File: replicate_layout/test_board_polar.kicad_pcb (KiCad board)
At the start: 2 copper layers, 30 parts, among them J1001 Pusa_4mm, J1002 Pusa_4mm, Q1001 CSD19531KCS, Q1002 CSD19531KCS, Q1003 CSD19531KCS, Q2001 CSD19531KCS, Q2002 CSD19531KCS, Q3001 CSD19531KCS, Q3002 CSD19531KCS, Q4001 CSD19531KCS, Q4002 CSD19531KCS, U1001 LAUNCHXL-F28377S, U2001 IR2181, U3001 IR2181, U4001 IR2181

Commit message: polarna replikacija dela GUI še ne dela samo še zone je treba replicirati
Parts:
- moved Q4002 68.7 mm to (220.0, 154.0), turned to 240 degrees
- moved R4002 62.8 mm to (216.0, 151.6), turned to 330 degrees
- moved Q4001 58.4 mm to (225.4, 144.6), turned to 240 degrees
- moved R4001 51.2 mm to (221.3, 142.3), turned to 330 degrees
- moved C4002 49.6 mm to (214.7, 144.0), turned to 240 degrees
- moved U4001 44.8 mm to (209.9, 142.3), turned to 330 degrees
- moved D4001 39.8 mm to (211.8, 139.0), turned to 150 degrees
- moved C4001 38.3 mm to (205.4, 138.6), turned to 240 degrees
- moved Q3002 27.6 mm to (222.9, 110.5), turned to 300 degrees
- moved Q3001 23.9 mm to (217.5, 101.2), turned to 300 degrees
- moved R3002 23.7 mm to (218.8, 112.9), turned to 30 degrees
- moved R3001 19.3 mm to (213.4, 103.5), turned to 30 degrees
- moved C3002 16.4 mm to (211.6, 110.2), turned to 300 degrees
- moved U3001 12.9 mm to (207.7, 113.4), turned to 30 degrees
- moved D3001 10.5 mm to (205.8, 110.1), turned to 210 degrees
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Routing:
- net (no net): track 0.00 -> 19.9 mm
- net /Veja_2/OUT: track 28.1 -> 44.0 mm
- net +VDC: track 27.2 -> 39.8 mm
- net GND: track 147.8 -> 158.6 mm
- net /Veja_3/OUT: track 40.2 -> 44.0 mm
- removed copper zone on F.Cu, net /Veja_1/OUT
- removed copper zone on F.Cu, net /Veja_2/OUT
- removed copper zone on F.Cu, net /Veja_3/OUT
- removed copper zone on F.Cu, net GND

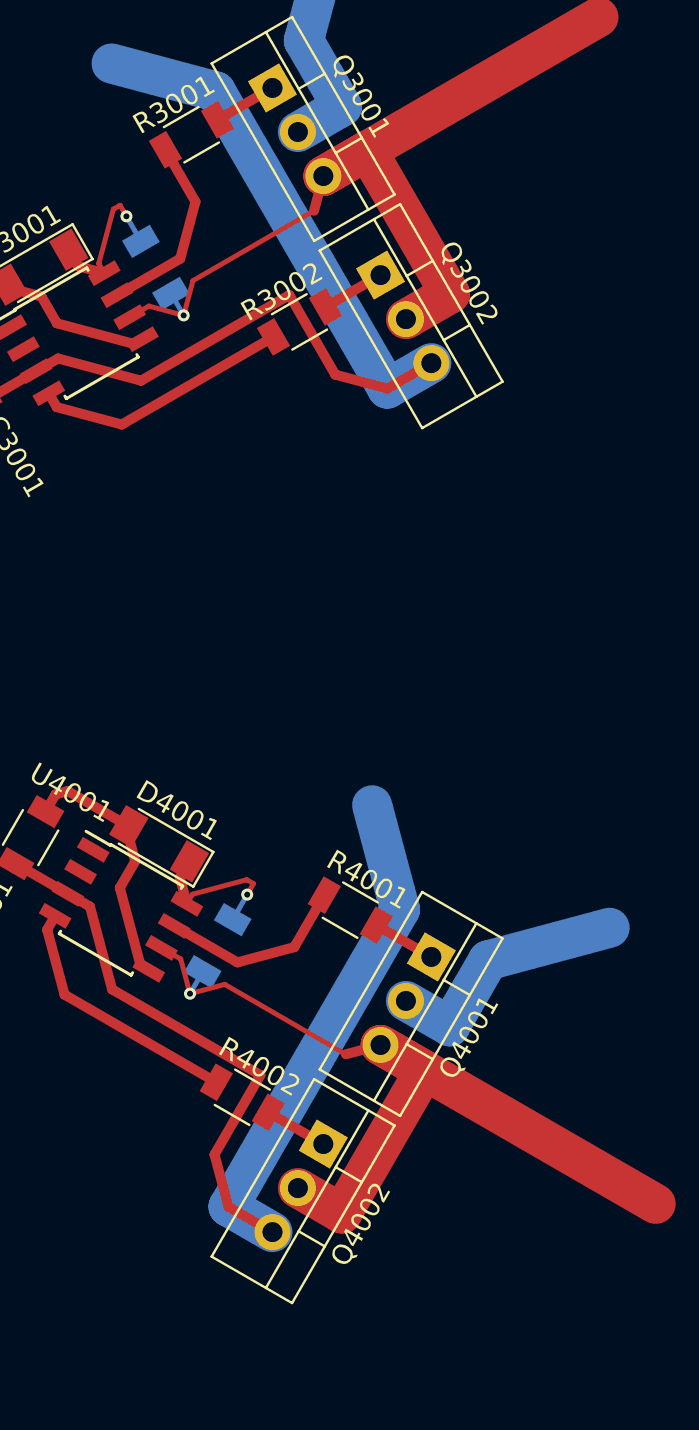
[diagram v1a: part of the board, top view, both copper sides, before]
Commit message: fixed a bug in test function changed how bounding box is calculated
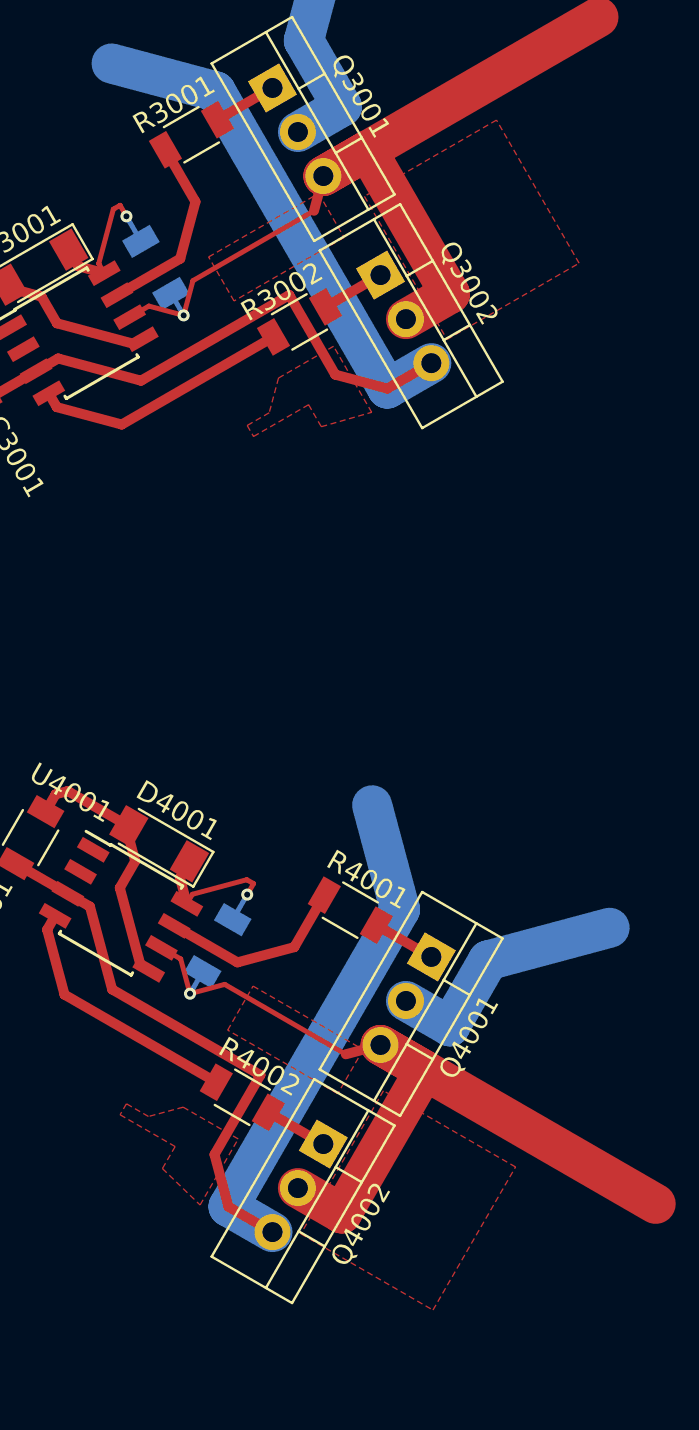
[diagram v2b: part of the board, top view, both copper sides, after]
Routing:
- added copper zone on F.Cu, net /Veja_2/OUT
- added copper zone on F.Cu, net /Veja_3/OUT
- added copper zone on F.Cu, net GND
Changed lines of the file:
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@@
-(kicad_pcb (version 20170919) (host pcbnew "(revision)-makepkg")
+(kicad_pcb (version 20170919) (host pcbnew "(2017-09-19 revision dddaa7e69)-makepkg")
   (general
     (thickness 1.6)
@@
   (segment (start 186.69 101.29) (end 184.315 103.665) (width 0.5) (layer F.Cu) (net 25))
   (segment (start 184.315 103.665) (end 183.515 103.665) (width 0.5) (layer F.Cu) (net 25))
+  (zone (net 4) (net_name /Veja_2/OUT) (layer F.Cu) (hatch edge 0.508)
+    (connect_pads (clearance 0.508))
+    (min_thickness 0.254)
+    (fill (arc_segments 16) (thermal_gap 0.508) (thermal_bridge_width 0.508))
+    (polygon
+      (pts
+        (xy 219.767651 106.459008) (xy 221.037651 108.658713) (xy 215.53839 111.833713) (xy 214.26839 109.634008)
+      )
+    )
+  )
+  (zone (net 2) (net_name GND) (layer F.Cu) (hatch edge 0.508)
+    (connect_pads (clearance 0.508))
+    (min_thickness 0.254)
+    (fill (arc_segments 16) (thermal_gap 0.508) (thermal_bridge_width 0.508))
+    (polygon
+      (pts
+        (xy 215.748021 153.698195) (xy 212.99839 152.110695) (xy 211.263538 152.575548) (xy 210.163685 151.940548) (xy 209.846185 152.490474)
+        (xy 212.595816 154.077974) (xy 211.960816 155.177826) (xy 213.843021 156.997752)
+      )
+    )
+  )
+  (zone (net 13) (net_name /Veja_3/OUT) (layer F.Cu) (hatch edge 0.508)
+    (connect_pads (clearance 0.508))
+    (min_thickness 0.254)
+    (fill (arc_segments 16) (thermal_gap 0.508) (thermal_bridge_width 0.508))
+    (polygon
+      (pts
+        (xy 229.604043 155.09886) (xy 223.00493 151.28886) (xy 218.87743 158.4379) (xy 225.476543 162.2479)
+      )
+    )
+  )
+  (zone (net 13) (net_name /Veja_3/OUT) (layer F.Cu) (hatch edge 0.508)
+    (connect_pads (clearance 0.508))
+    (min_thickness 0.254)
+    (fill (arc_segments 16) (thermal_gap 0.508) (thermal_bridge_width 0.508))
+    (polygon
+      (pts
+        (xy 221.990151 149.236508) (xy 220.720151 151.436213) (xy 215.22089 148.261213) (xy 216.49089 146.061508)
+      )
+    )
+  )
+  (zone (net 2) (net_name GND) (layer F.Cu) (hatch edge 0.508)
+    (connect_pads (clearance 0.508))
+    (min_thickness 0.254)
+    (fill (arc_segments 16) (thermal_gap 0.508) (thermal_bridge_width 0.508))
+    (polygon
+      (pts
+        (xy 220.510521 114.095695) (xy 217.76089 115.683195) (xy 217.296038 117.418048) (xy 216.196185 118.053048) (xy 216.513685 118.602974)
+        (xy 219.263316 117.015474) (xy 219.898316 118.115326) (xy 222.415521 117.395252)
+      )
+    )
+  )
+  (zone (net 4) (net_name /Veja_2/OUT) (layer F.Cu) (hatch edge 0.508)
+    (connect_pads (clearance 0.508))
+    (min_thickness 0.254)
+    (fill (arc_segments 16) (thermal_gap 0.508) (thermal_bridge_width 0.508))
+    (polygon
+      (pts
+        (xy 228.651543 102.79636) (xy 222.05243 106.60636) (xy 226.17993 113.7554) (xy 232.779043 109.9454)
+      )
+    )
+  )
 )

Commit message: Updated documentation
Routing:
- added copper zone on F.Cu, net /Veja_1/OUT
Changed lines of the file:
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@@
     (connect_pads (clearance 0.508))
     (min_thickness 0.254)
-    (fill (arc_segments 16) (thermal_gap 0.508) (thermal_bridge_width 0.508))
+    (fill yes (arc_segments 16) (thermal_gap 0.508) (thermal_bridge_width 0.508))
     (polygon
       (pts
-        (xy 220.510521 114.095695) (xy 217.76089 115.683195) (xy 217.296038 117.418048) (xy 216.196185 118.053048) (xy 216.513685 118.602974)
-        (xy 219.263316 117.015474) (xy 219.898316 118.115326) (xy 222.415521 117.395252)
+        (xy 188.595 90.17) (xy 188.595 93.345) (xy 189.865 94.615) (xy 189.865 95.885) (xy 190.5 95.885)
+        (xy 190.5 92.71) (xy 191.77 92.71) (xy 192.405 90.17)
       )
     )
@@
       )
     )
+  )
+  (zone (net 2) (net_name GND) (layer F.Cu) (hatch edge 0.508)
+    (connect_pads (clearance 0.508))
+    (min_thickness 0.254)
+    (fill (arc_segments 16) (thermal_gap 0.508) (thermal_bridge_width 0.508))
+    (polygon
+      (pts
+        (xy 220.510521 114.095695) (xy 217.76089 115.683195) (xy 217.296038 117.418048) (xy 216.196185 118.053048) (xy 216.513685 118.602974)
+        (xy 219.263316 117.015474) (xy 219.898316 118.115326) (xy 222.415521 117.395252)
+      )
+    )
+  )
+  (zone (net 3) (net_name /Veja_1/OUT) (layer F.Cu) (hatch edge 0.508)
+    (connect_pads (clearance 0.508))
+    (min_thickness 0.254)
+    (fill yes (arc_segments 16) (thermal_gap 0.508) (thermal_bridge_width 0.508))
+    (polygon
+      (pts
+        (xy 181.61 86.995) (xy 184.15 86.995) (xy 184.15 93.345) (xy 181.61 93.345)
+      )
+    )
+  )
+  (zone (net 3) (net_name /Veja_1/OUT) (layer F.Cu) (hatch edge 0.508)
+    (connect_pads (clearance 0.508))
+    (min_thickness 0.254)
+    (fill yes (arc_segments 16) (thermal_gap 0.508) (thermal_bridge_width 0.508))
+    (polygon
+      (pts
+        (xy 182.88 77.47) (xy 182.88 85.09) (xy 191.135 85.09) (xy 191.135 77.47)
+      )
+    )

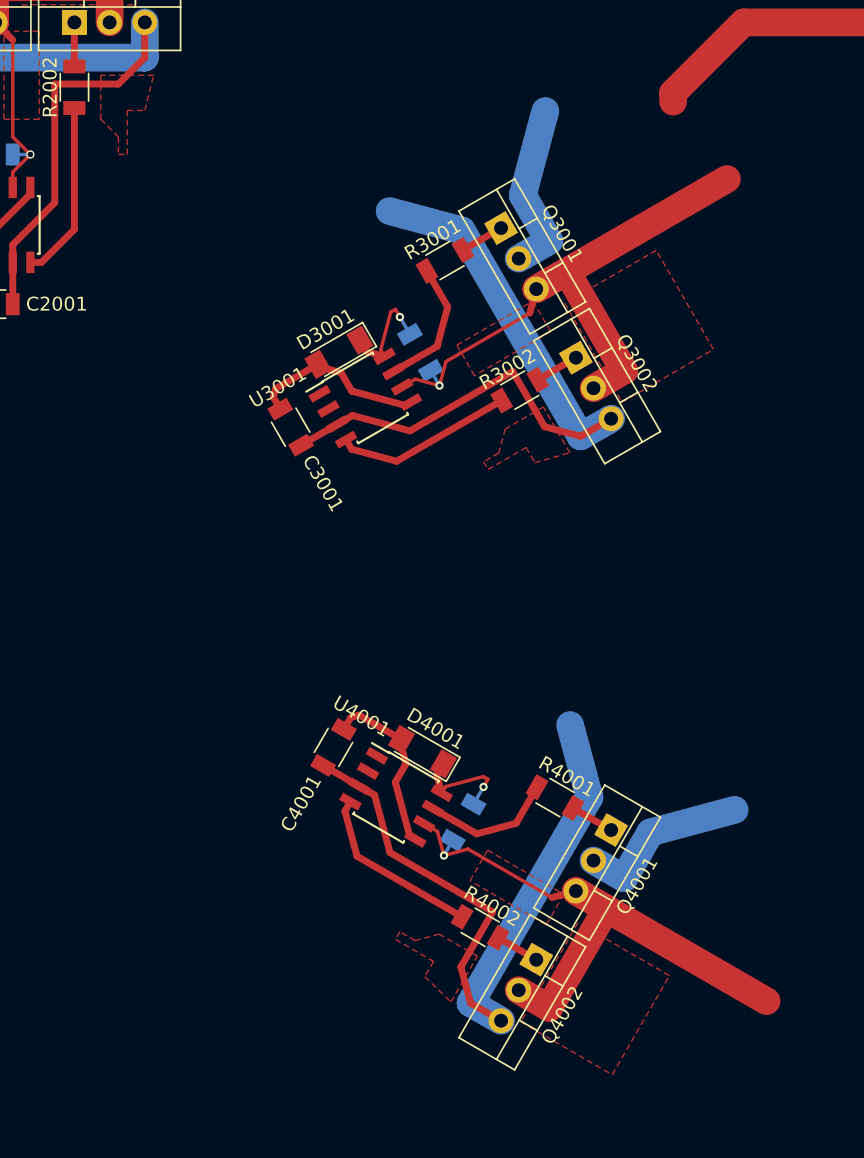
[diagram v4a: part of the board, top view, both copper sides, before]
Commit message: Bugfix for circular module orientation in linear replication
Updated test layouts as it tests for non copper zones also
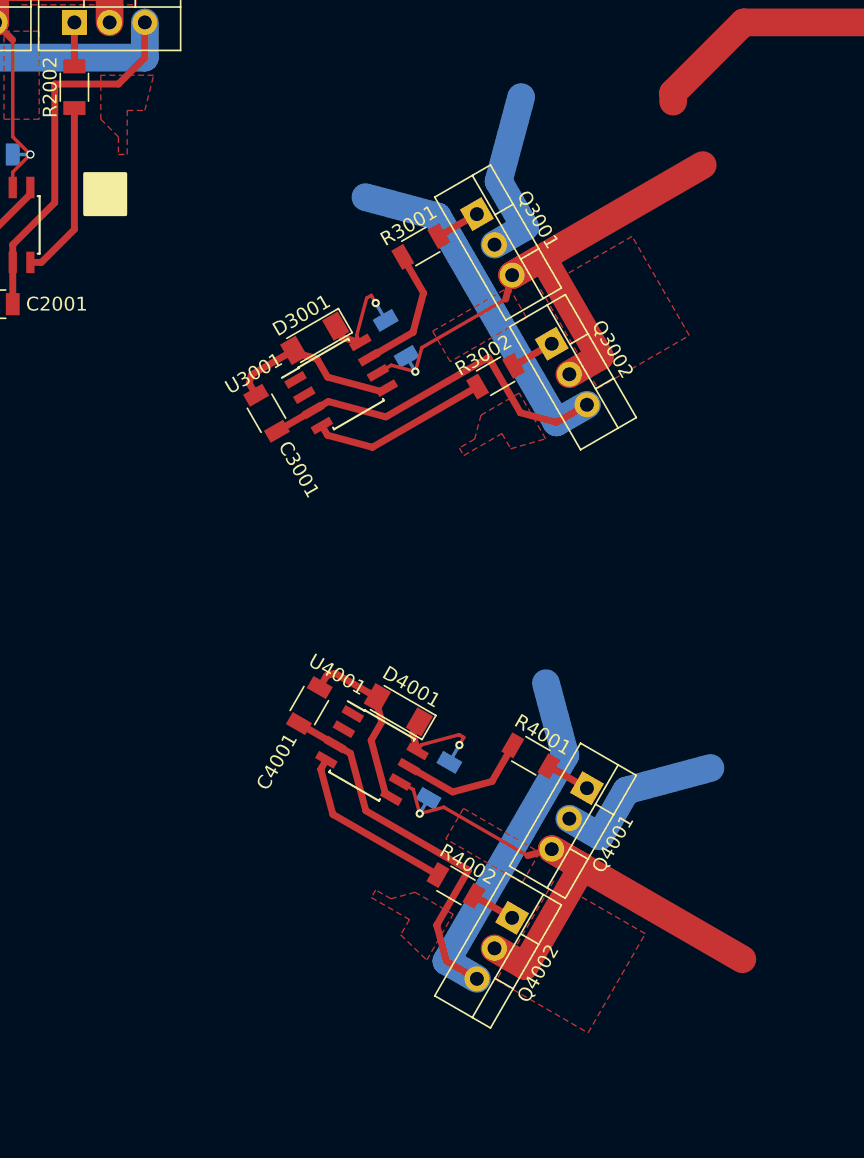
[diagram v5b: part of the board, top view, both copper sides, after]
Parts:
- moved R4001 3.49 mm to (219.6, 139.2)
- moved Q4001 3.49 mm to (223.7, 141.6)
- moved R4002 3.49 mm to (214.2, 148.6)
- moved D4001 3.49 mm to (210.1, 135.9)
- moved C4001 3.49 mm to (203.6, 135.6)
- moved C4002 3.49 mm to (213.0, 141.0)
- moved Q4002 3.49 mm to (218.3, 150.9)
- moved U4001 3.49 mm to (208.1, 139.2)
- moved R3001 2.01 mm to (211.7, 102.5)
- moved R3002 2.01 mm to (217.1, 111.9)
- moved Q3001 2.01 mm to (215.7, 100.2)
- moved C3001 2.01 mm to (200.5, 114.5)
- moved C3002 2.01 mm to (209.9, 109.1)
- moved D3001 2.01 mm to (204.0, 109.1)
- moved Q3002 2.01 mm to (221.1, 109.5)
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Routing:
- net +VDC: track 39.8 -> 59.7 mm
- net (no net): track 19.9 -> 0.00 mm
